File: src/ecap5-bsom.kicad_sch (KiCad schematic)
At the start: 0 parts

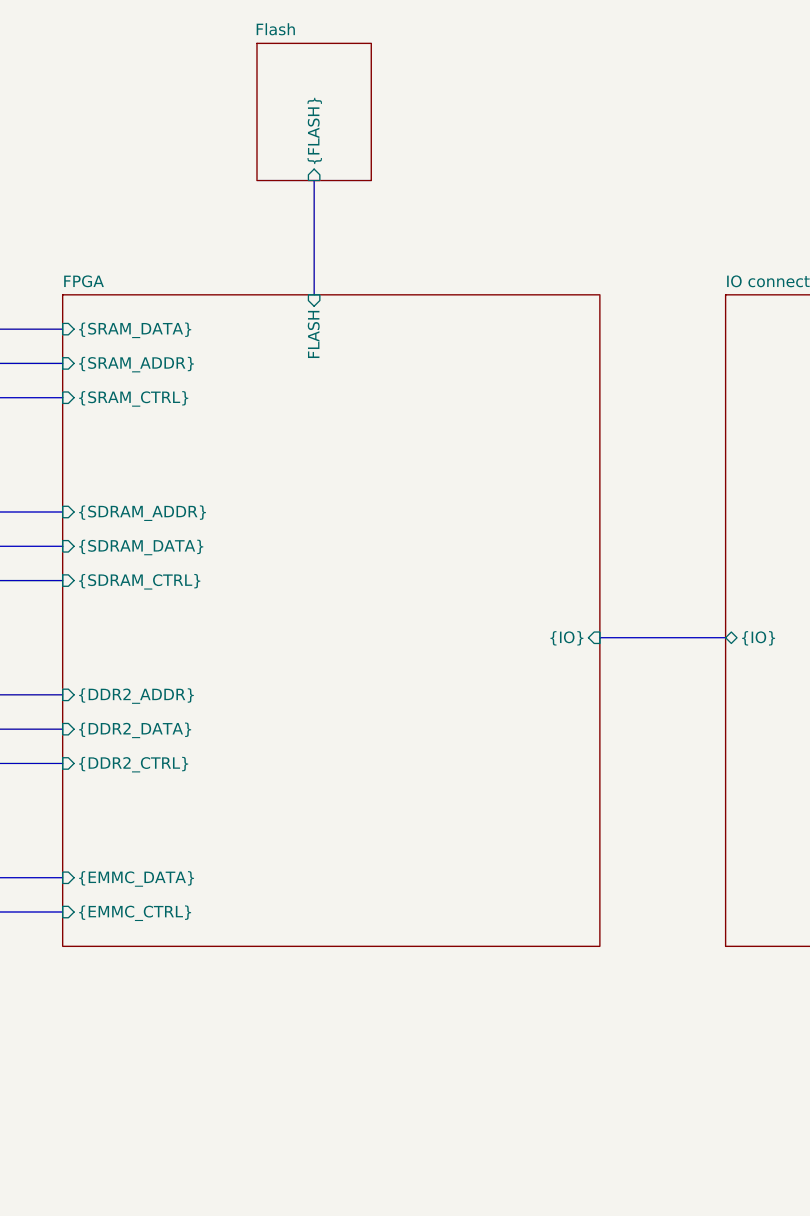
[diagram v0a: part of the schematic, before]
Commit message: Adds the clock oscillator
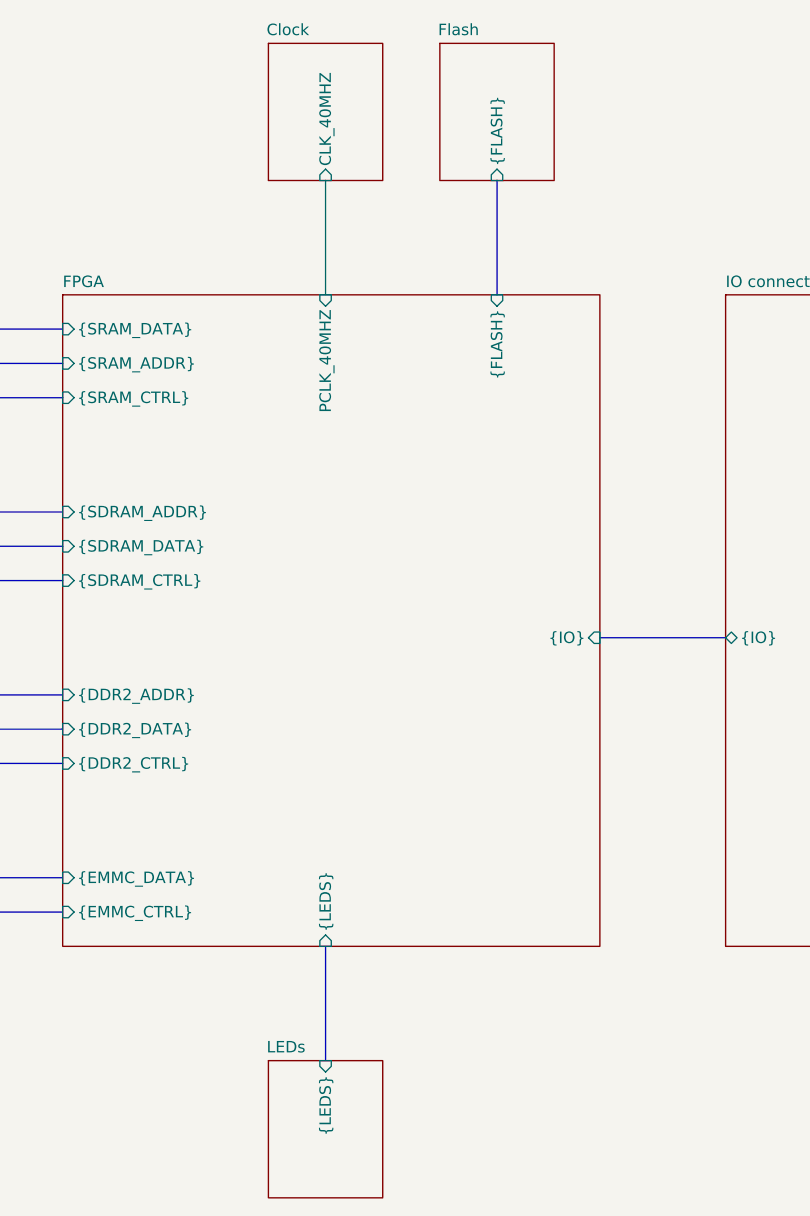
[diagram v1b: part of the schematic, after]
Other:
- added sheet Clock (schematics/clock.kicad_sch)
- added sheet LEDs (schematics/leds.kicad_sch)
- sheet FPGA ports: added PCLK_40MHZ, {FLASH}, {LEDS}; removed FLASH
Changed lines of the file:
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@@
+	(bus
+		(pts
+			(xy 153.67 133.35) (xy 153.67 146.05)
+		)
+		(stroke
+			(width 0)
+			(type default)
+		)
+	)
 	(bus
 		(pts
@@
 		)
 	)
+	(wire
+		(pts
+			(xy 153.67 48.26) (xy 153.67 60.96)
+		)
+		(stroke
+			(width 0)
+			(type default)
+		)
+	)
 	(bus
 		(pts
@@
 	(bus
 		(pts
-			(xy 152.4 48.26) (xy 152.4 60.96)
+			(xy 172.72 48.26) (xy 172.72 60.96)
 		)
 		(stroke
@@
 			(project "ecap5-bsom"
 				(path "/c5fd18a3-9aa0-4151-b6e0-94da3d606686"
-					(page "14")
-				)
-			)
-		)
-	)
-	(sheet
-		(at 146.05 33.02)
+					(page "16")
+				)
+			)
+		)
+	)
+	(sheet
+		(at 166.37 33.02)
 		(size 12.7 15.24)
 		(stroke
@@
 		)
 		(property "Sheetname" "Flash"
-			(at 145.8464 32.258 0)
+			(at 166.1664 32.258 0)
 			(effects
 				(font
@@
 		)
 		(property "Sheetfile" "schematics/flash.kicad_sch"
-			(at 159.3346 48.26 90)
+			(at 179.6546 48.26 90)
 			(effects
 				(font
@@
 		)
 		(pin "{FLASH}" input
-			(at 152.4 48.26 270)
-			(effects
-				(font
-					(size 1.27 1.27)
-				)
-				(justify left)
-			)
-		)
-		(instances
-			(project "ecap5-bsom"
-				(path "/c5fd18a3-9aa0-4151-b6e0-94da3d606686"
-					(page "11")
+			(at 172.72 48.26 270)
+			(effects
+				(font
+					(size 1.27 1.27)
+				)
+				(justify left)
+			)
+		)
+		(instances
+			(project "ecap5-bsom"
+				(path "/c5fd18a3-9aa0-4151-b6e0-94da3d606686"
+					(page "13")
 				)
 			)
@@
 			(project "ecap5-bsom"
 				(path "/c5fd18a3-9aa0-4151-b6e0-94da3d606686"
-					(page "16")
+					(page "18")
 				)
 			)
@@
 			(project "ecap5-bsom"
 				(path "/c5fd18a3-9aa0-4151-b6e0-94da3d606686"
-					(page "12")
+					(page "14")
 				)
 			)
@@
 			(project "ecap5-bsom"
 				(path "/c5fd18a3-9aa0-4151-b6e0-94da3d606686"
-					(page "13")
+					(page "15")
 				)
 			)
@@
 	)
 	(sheet
+		(at 147.32 33.02)
+		(size 12.7 15.24)
+		(stroke
+			(width 0.1524)
+			(type solid)
+		)
+		(fill
+			(color 0 0 0 0.0000)
+		)
+		(property "Sheetname" "Clock"
+			(at 147.1164 32.258 0)
+			(effects
+				(font
+					(size 1.27 1.27)
+				)
+				(justify left bottom)
+			)
+		)
+		(property "Sheetfile" "schematics/clock.kicad_sch"
+			(at 160.6046 48.26 90)
+			(effects
+				(font
+					(size 1.27 1.27)
+				)
+				(justify left top)
+				(hide yes)
+			)
+		)
+		(pin "CLK_40MHZ" input
+			(at 153.67 48.26 270)
+			(effects
+				(font
+					(size 1.27 1.27)
+				)
+				(justify left)
+			)
+		)
+		(instances
+			(project "ecap5-bsom"
+				(path "/c5fd18a3-9aa0-4151-b6e0-94da3d606686"
+					(page "12")
+				)
+			)
+		)
+	)
+	(sheet
 		(at 71.12 121.92)
 		(size 29.21 11.43)
@@
 			(project "ecap5-bsom"
 				(path "/c5fd18a3-9aa0-4151-b6e0-94da3d606686"
-					(page "15")
+					(page "17")
 				)
 			)
@@
 			)
 		)
-		(pin "FLASH" input
-			(at 152.4 60.96 90)
-			(effects
-				(font
-					(size 1.27 1.27)
-				)
-				(justify right)
+		(pin "{FLASH}" input
+			(at 172.72 60.96 90)
+			(effects
+				(font
+					(size 1.27 1.27)
+				)
+				(justify right)
+			)
+		)
+		(pin "PCLK_40MHZ" input
+			(at 153.67 60.96 90)
+			(effects
+				(font
+					(size 1.27 1.27)
+				)
+				(justify right)
+			)
+		)
+		(pin "{LEDS}" input
+			(at 153.67 133.35 270)
+			(effects
+				(font
+					(size 1.27 1.27)
+				)
+				(justify left)
 			)
 		)
@@
 				)
 			)
+		)
+	)
+	(sheet
+		(at 147.32 146.05)
+		(size 12.7 15.24)
+		(stroke
+			(width 0.1524)
+			(type solid)
+		)
+		(fill
+			(color 0 0 0 0.0000)
+		)
+		(property "Sheetname" "LEDs"
+			(at 147.1164 145.288 0)
+			(effects
+				(font
+					(size 1.27 1.27)
+				)
+				(justify left bottom)
+			)
+		)
+		(property "Sheetfile" "schematics/leds.kicad_sch"
+			(at 160.6046 161.29 90)
+			(effects
+				(font
+					(size 1.27 1.27)
+				)
+				(justify left top)
+				(hide yes)
+			)
+		)
+		(pin "{LEDS}" input
+			(at 153.67 146.05 90)
+			(effects
+				(font
+					(size 1.27 1.27)
+				)
+				(justify right)
+			)
+		)
+		(instances
+			(project "ecap5-bsom"
+				(path "/c5fd18a3-9aa0-4151-b6e0-94da3d606686"
+					(page "21")
+				)
+			)

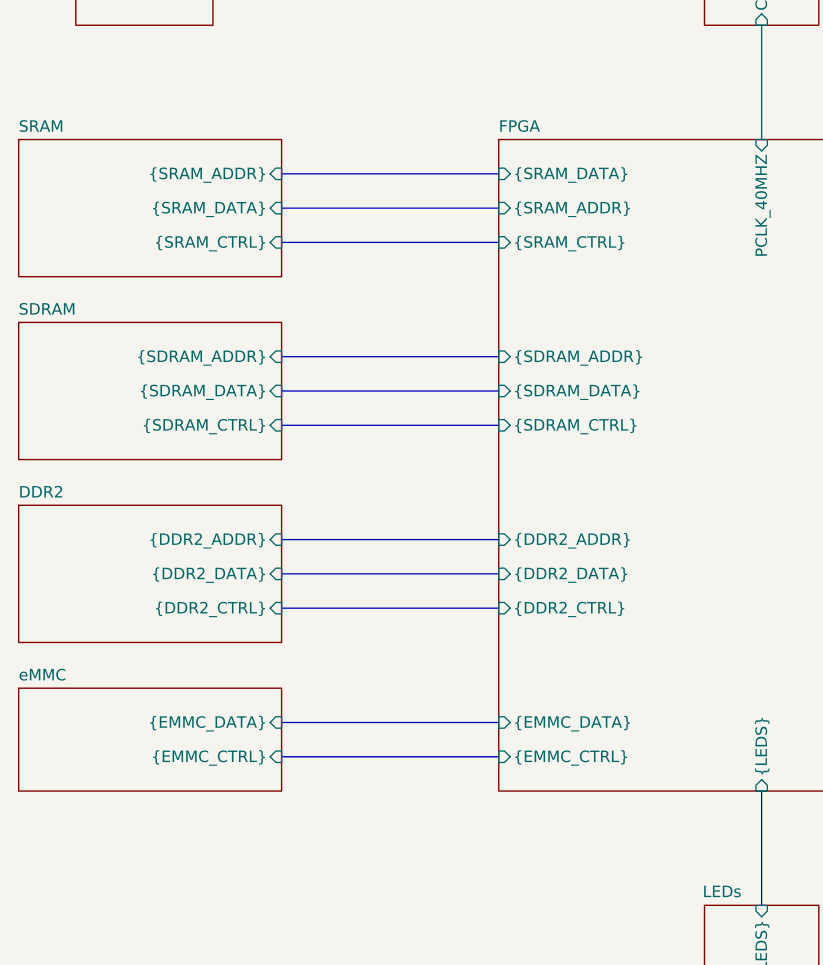
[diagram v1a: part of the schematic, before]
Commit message: Adds bus aliases
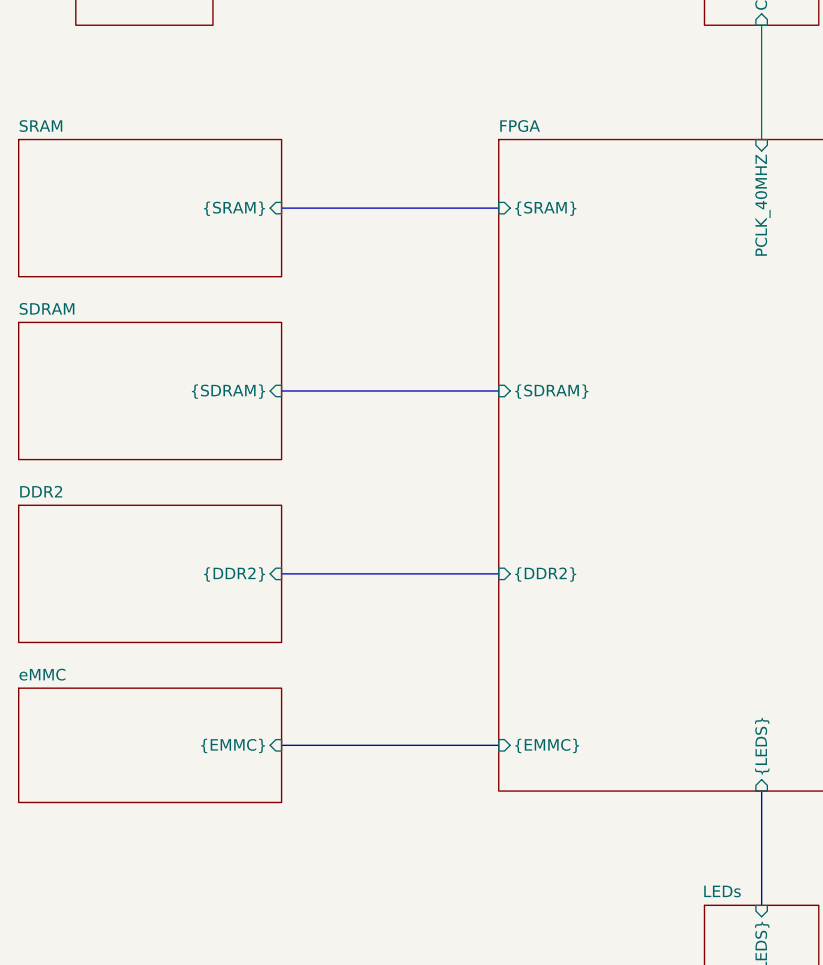
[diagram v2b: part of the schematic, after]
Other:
- sheet DDR2 ports: added {DDR2}; removed {DDR2_ADDR}, {DDR2_CTRL}, {DDR2_DATA}
- sheet FPGA ports: added {DDR2}, {EMMC}, {SDRAM}, {SRAM}; removed {DDR2_ADDR}, {DDR2_CTRL}, {DDR2_DATA}, {EMMC_CTRL}, {EMMC_DATA}, {SDRAM_ADDR}, {SDRAM_CTRL}, {SDRAM_DATA}, {SRAM_ADDR}, {SRAM_CTRL}, {SRAM_DATA}
- sheet SDRAM ports: added {SDRAM}; removed {SDRAM_ADDR}, {SDRAM_CTRL}, {SDRAM_DATA}
- sheet SRAM ports: added {SRAM}; removed {SRAM_ADDR}, {SRAM_CTRL}, {SRAM_DATA}
- sheet eMMC ports: added {EMMC}; removed {EMMC_CTRL}, {EMMC_DATA}
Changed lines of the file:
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@@
+	(bus
+		(pts
+			(xy 100.33 109.22) (xy 124.46 109.22)
+		)
+		(stroke
+			(width 0)
+			(type default)
+		)
+	)
 	(bus
 		(pts
@@
 	(bus
 		(pts
-			(xy 100.33 92.71) (xy 124.46 92.71)
+			(xy 100.33 68.58) (xy 124.46 68.58)
 		)
 		(stroke
@@
 	(bus
 		(pts
-			(xy 100.33 105.41) (xy 124.46 105.41)
-		)
-		(stroke
-			(width 0)
-			(type default)
-		)
-	)
-	(bus
-		(pts
 			(xy 184.15 99.06) (xy 198.12 99.06)
 		)
@@
 	(bus
 		(pts
-			(xy 100.33 68.58) (xy 124.46 68.58)
-		)
-		(stroke
-			(width 0)
-			(type default)
-		)
-	)
-	(bus
-		(pts
-			(xy 100.33 109.22) (xy 124.46 109.22)
+			(xy 100.33 128.27) (xy 124.46 128.27)
 		)
 		(stroke
@@
 	(bus
 		(pts
-			(xy 100.33 85.09) (xy 124.46 85.09)
-		)
-		(stroke
-			(width 0)
-			(type default)
-		)
-	)
-	(bus
-		(pts
-			(xy 100.33 129.54) (xy 124.46 129.54)
-		)
-		(stroke
-			(width 0)
-			(type default)
-		)
-	)
-	(bus
-		(pts
 			(xy 172.72 48.26) (xy 172.72 60.96)
-		)
-		(stroke
-			(width 0)
-			(type default)
-		)
-	)
-	(bus
-		(pts
-			(xy 100.33 64.77) (xy 124.46 64.77)
-		)
-		(stroke
-			(width 0)
-			(type default)
-		)
-	)
-	(bus
-		(pts
-			(xy 100.33 72.39) (xy 124.46 72.39)
-		)
-		(stroke
-			(width 0)
-			(type default)
-		)
-	)
-	(bus
-		(pts
-			(xy 100.33 125.73) (xy 124.46 125.73)
-		)
-		(stroke
-			(width 0)
-			(type default)
-		)
-	)
-	(bus
-		(pts
-			(xy 100.33 113.03) (xy 124.46 113.03)
 		)
 		(stroke
@@
 			)
 		)
-		(pin "{DDR2_ADDR}" input
-			(at 100.33 105.41 0)
-			(effects
-				(font
-					(size 1.27 1.27)
-				)
-				(justify right)
-			)
-		)
-		(pin "{DDR2_CTRL}" input
-			(at 100.33 113.03 0)
-			(effects
-				(font
-					(size 1.27 1.27)
-				)
-				(justify right)
-			)
-		)
-		(pin "{DDR2_DATA}" input
+		(pin "{DDR2}" input
 			(at 100.33 109.22 0)
 			(effects
@@
 			)
 		)
-		(pin "{SRAM_CTRL}" input
-			(at 100.33 72.39 0)
-			(effects
-				(font
-					(size 1.27 1.27)
-				)
-				(justify right)
-			)
-		)
-		(pin "{SRAM_DATA}" input
+		(pin "{SRAM}" input
 			(at 100.33 68.58 0)
-			(effects
-				(font
-					(size 1.27 1.27)
-				)
-				(justify right)
-			)
-		)
-		(pin "{SRAM_ADDR}" input
-			(at 100.33 64.77 0)
 			(effects
 				(font
@@
 			)
 		)
-		(pin "{SDRAM_ADDR}" input
-			(at 100.33 85.09 0)
-			(effects
-				(font
-					(size 1.27 1.27)
-				)
-				(justify right)
-			)
-		)
-		(pin "{SDRAM_CTRL}" input
-			(at 100.33 92.71 0)
-			(effects
-				(font
-					(size 1.27 1.27)
-				)
-				(justify right)
-			)
-		)
-		(pin "{SDRAM_DATA}" input
+		(pin "{SDRAM}" input
 			(at 100.33 88.9 0)
 			(effects
@@
 	(sheet
 		(at 71.12 121.92)
-		(size 29.21 11.43)
+		(size 29.21 12.7)
 		(fields_autoplaced yes)
 		(stroke
@@
 		)
 		(property "Sheetfile" "schematics/emmc.kicad_sch"
-			(at 71.12 133.9346 0)
-			(effects
-				(font
-					(size 1.27 1.27)
-				)
-				(justify left top)
-				(hide yes)
-			)
-		)
-		(pin "{EMMC_DATA}" input
-			(at 100.33 125.73 0)
-			(effects
-				(font
-					(size 1.27 1.27)
-				)
-				(justify right)
-			)
-		)
-		(pin "{EMMC_CTRL}" input
-			(at 100.33 129.54 0)
+			(at 71.12 135.2046 0)
+			(effects
+				(font
+					(size 1.27 1.27)
+				)
+				(justify left top)
+				(hide yes)
+			)
+		)
+		(pin "{EMMC}" input
+			(at 100.33 128.27 0)
 			(effects
 				(font
@@
 			)
 		)
-		(pin "{DDR2_ADDR}" input
-			(at 124.46 105.41 180)
-			(effects
-				(font
-					(size 1.27 1.27)
-				)
-				(justify left)
-			)
-		)
-		(pin "{SDRAM_DATA}" input
+		(pin "{SDRAM}" input
 			(at 124.46 88.9 180)
 			(effects
@@
 			)
 		)
-		(pin "{SDRAM_ADDR}" input
-			(at 124.46 85.09 180)
-			(effects
-				(font
-					(size 1.27 1.27)
-				)
-				(justify left)
-			)
-		)
-		(pin "{SDRAM_CTRL}" input
-			(at 124.46 92.71 180)
-			(effects
-				(font
-					(size 1.27 1.27)
-				)
-				(justify left)
-			)
-		)
-		(pin "{DDR2_CTRL}" input
-			(at 124.46 113.03 180)
-			(effects
-				(font
-					(size 1.27 1.27)
-				)
-				(justify left)
-			)
-		)
-		(pin "{DDR2_DATA}" input
+		(pin "{DDR2}" input
 			(at 124.46 109.22 180)
 			(effects
@@
 			)
 		)
-		(pin "{EMMC_DATA}" input
-			(at 124.46 125.73 180)
-			(effects
-				(font
-					(size 1.27 1.27)
-				)
-				(justify left)
-			)
-		)
-		(pin "{EMMC_CTRL}" input
-			(at 124.46 129.54 180)
-			(effects
-				(font
-					(size 1.27 1.27)
-				)
-				(justify left)
-			)
-		)
-		(pin "{SRAM_CTRL}" input
-			(at 124.46 72.39 180)
-			(effects
-				(font
-					(size 1.27 1.27)
-				)
-				(justify left)
-			)
-		)
-		(pin "{SRAM_ADDR}" input
+		(pin "{EMMC}" input
+			(at 124.46 128.27 180)
+			(effects
+				(font
+					(size 1.27 1.27)
+				)
+				(justify left)
+			)
+		)
+		(pin "{SRAM}" input
 			(at 124.46 68.58 180)
 			(effects
 				(font
-					(size 1.27 1.27)
-				)
-				(justify left)
-			)
-		)
-		(pin "{SRAM_DATA}" input
-			(at 124.46 64.77 180)
-			(effects
-				(font
